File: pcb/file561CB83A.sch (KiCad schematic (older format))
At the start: 50 parts, among them P8 CONN_01X02, P9 CONN_01X02, Q2 BC849, Q3 IRF9530, Q4 CSD18536KCS, Q5 BC849, Q6 BC849, Q7 IRF9530, Q8 CSD18536KCS, Q9 BC849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

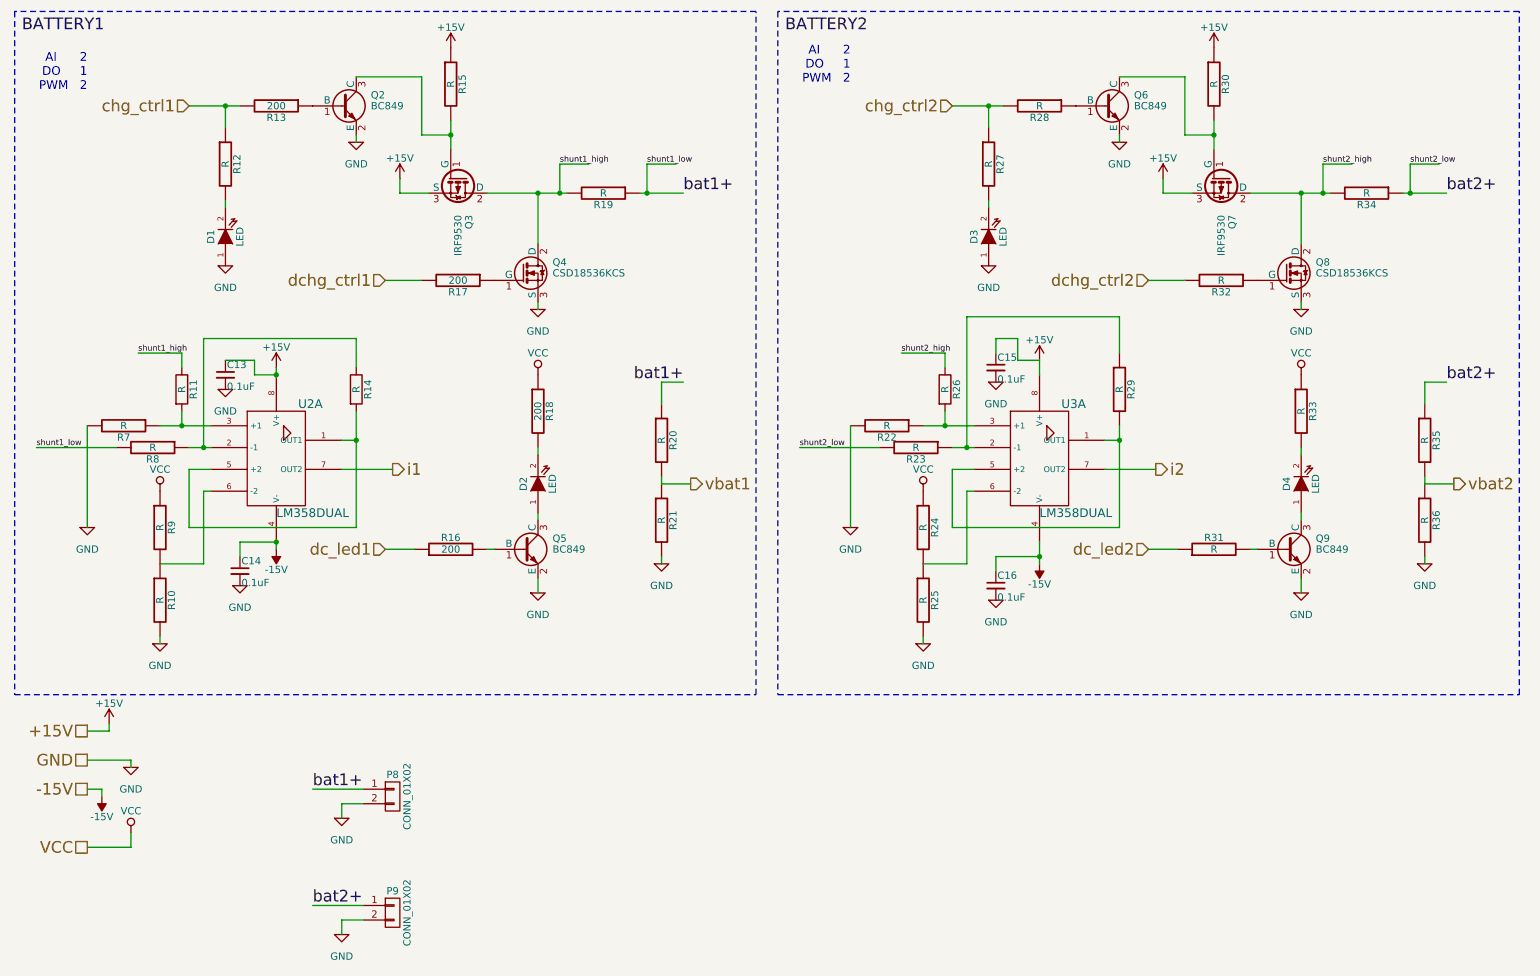
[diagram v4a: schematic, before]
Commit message: Changed fan FET (Q22). Many other minor layout changes. Production candidate.
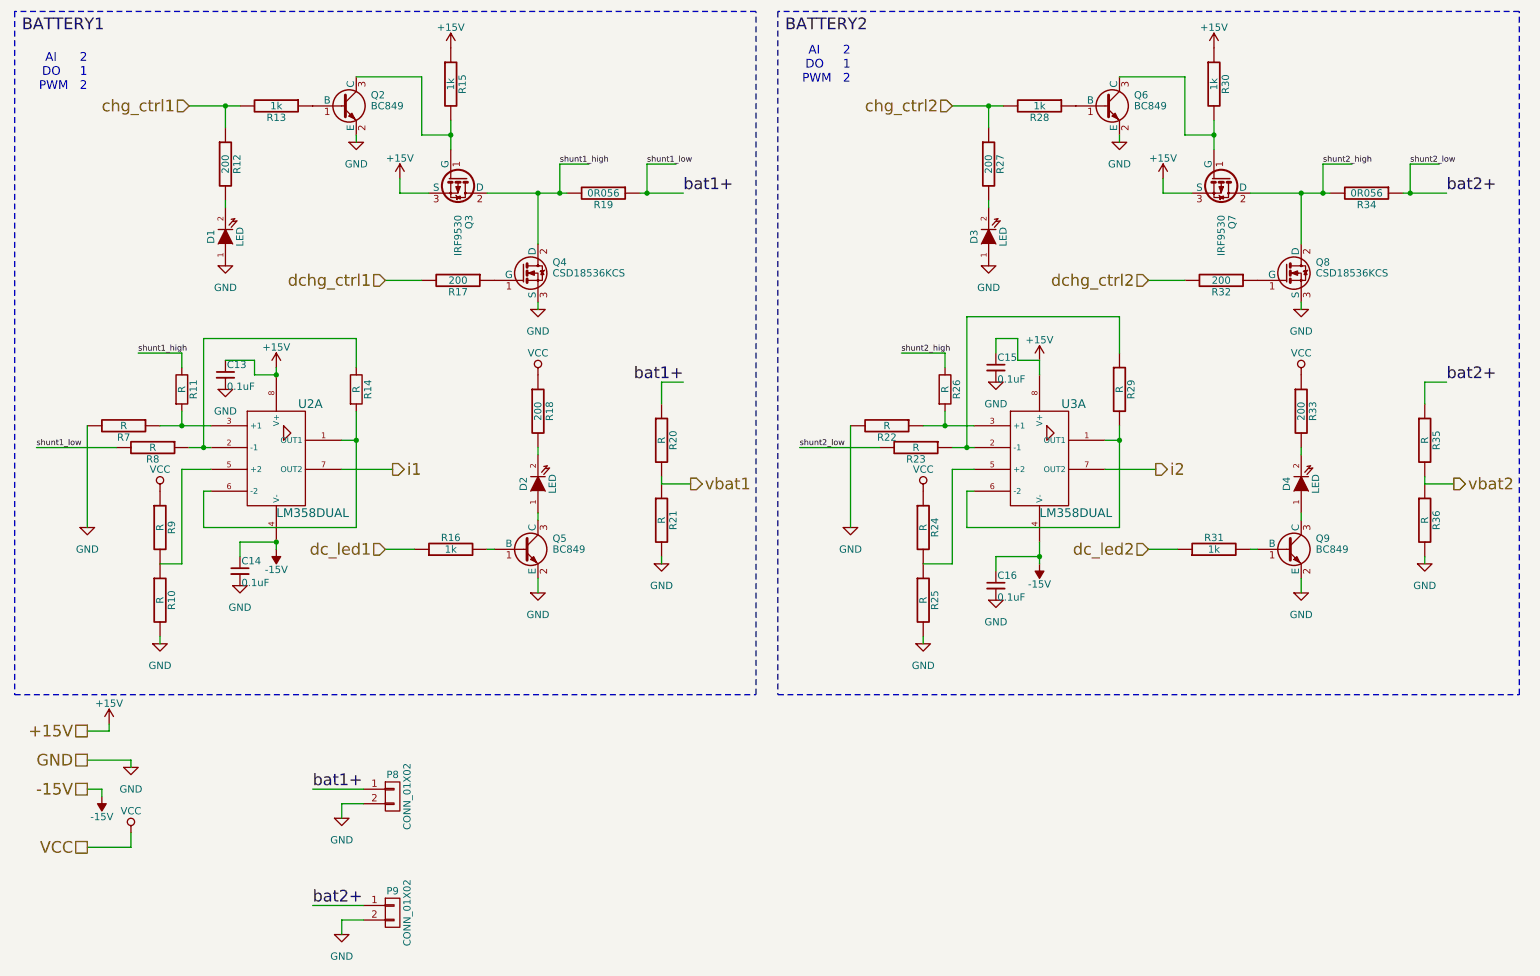
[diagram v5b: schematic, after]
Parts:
- Q3, Q4, Q7, Q8: footprint Power_Integrations:TO-220 -> Custom Footprints:TO-220
- R12, R27, R32, R33: value R -> 200
- R13, R16: value 200 -> 1k
- R15, R28, R30, R31: value R -> 1k
- R19, R34: value R -> 0R056
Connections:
- net at R14.2, U2.1 (OUT1): now also U2.6 (-2); no longer U2.5 (+2)
- net at R10.1, R9.2: now also U2.5 (+2); no longer U2.6 (-2)
- net at R29.2, U3.1 (OUT1): now also U3.6 (-2); no longer U3.5 (+2)
- net at R24.2, R25.1: now also U3.5 (+2); no longer U3.6 (-2)
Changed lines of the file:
@@
 F 0 "Q4" H 4300 2425 50  0000 L CNN
 F 1 "CSD18536KCS" H 4300 2350 50  0000 L CNN
-F 2 "Power_Integrations:TO-220" H 4300 2275 50  0001 L CIN
+F 2 "Custom Footprints:TO-220" H 4300 2275 50  0001 L CIN
 F 3 "" H 4100 2350 50  0000 L CNN
 	1    4100 2350
@@
 F 0 "Q3" H 3900 1775 50  0000 L CNN
 F 1 "IRF9530" H 3900 1700 50  0000 L CNN
-F 2 "Power_Integrations:TO-220" H 3900 1625 50  0001 L CIN
+F 2 "Custom Footprints:TO-220" H 3900 1625 50  0001 L CIN
 F 3 "" H 3650 1700 50  0000 L CNN
 	1    3650 1700
@@
 P 2050 1600
 F 0 "R12" V 2130 1600 50  0000 C CNN
-F 1 "R" V 2050 1600 50  0000 C CNN
+F 1 "200" V 2050 1600 50  0000 C CNN
 F 2 "Resistors_SMD:R_0805_HandSoldering" V 1980 1600 30  0001 C CNN
 F 3 "" H 2050 1600 30  0000 C CNN
@@
 P 3600 1050
 F 0 "R15" V 3680 1050 50  0000 C CNN
-F 1 "R" V 3600 1050 50  0000 C CNN
+F 1 "1k" V 3600 1050 50  0000 C CNN
 F 2 "Resistors_SMD:R_0805_HandSoldering" V 3530 1050 30  0001 C CNN
 F 3 "" H 3600 1050 30  0000 C CNN
@@
 P 4650 1800
 F 0 "R19" V 4730 1800 50  0000 C CNN
-F 1 "R" V 4650 1800 50  0000 C CNN
+F 1 "0R056" V 4650 1800 50  0000 C CNN
 F 2 "Resistors_SMD:R_2512_HandSoldering" V 4580 1800 30  0001 C CNN
 F 3 "" H 4650 1800 30  0000 C CNN
@@
 P 2400 1200
 F 0 "R13" V 2480 1200 50  0000 C CNN
-F 1 "200" V 2400 1200 50  0000 C CNN
+F 1 "1k" V 2400 1200 50  0000 C CNN
 F 2 "Resistors_SMD:R_0805_HandSoldering" V 2330 1200 30  0001 C CNN
 F 3 "" H 2400 1200 30  0000 C CNN
@@
 P 3600 4250
 F 0 "R16" V 3680 4250 50  0000 C CNN
-F 1 "200" V 3600 4250 50  0000 C CNN
+F 1 "1k" V 3600 4250 50  0000 C CNN
 F 2 "Resistors_SMD:R_0805_HandSoldering" V 3530 4250 30  0001 C CNN
 F 3 "" H 3600 4250 30  0000 C CNN
@@
 	1300 3550 750  3550
 Wire Wire Line
-	2950 4100 1800 4100
-Wire Wire Line
-	1800 4100 1800 3700
-Wire Wire Line
-	1800 3700 1950 3700
+	2950 4100 1900 4100
+Wire Wire Line
+	1750 3700 1950 3700
 Connection ~ 2950 3500
 Wire Wire Line
 	1950 3850 1900 3850
-Wire Wire Line
-	1900 3850 1900 4350
-Wire Wire Line
-	1900 4350 1600 4350
 Wire Wire Line
 	1600 4900 1600 4850
@@
 F 0 "Q8" H 9550 2425 50  0000 L CNN
 F 1 "CSD18536KCS" H 9550 2350 50  0000 L CNN
-F 2 "Power_Integrations:TO-220" H 9550 2275 50  0001 L CIN
+F 2 "Custom Footprints:TO-220" H 9550 2275 50  0001 L CIN
 F 3 "" H 9350 2350 50  0000 L CNN
 	1    9350 2350
@@
 F 0 "Q7" H 9150 1775 50  0000 L CNN
 F 1 "IRF9530" H 9150 1700 50  0000 L CNN
-F 2 "Power_Integrations:TO-220" H 9150 1625 50  0001 L CIN
+F 2 "Custom Footprints:TO-220" H 9150 1625 50  0001 L CIN
 F 3 "" H 8900 1700 50  0000 L CNN
 	1    8900 1700
@@
 P 9450 3300
 F 0 "R33" V 9530 3300 50  0000 C CNN
-F 1 "R" V 9450 3300 50  0000 C CNN
+F 1 "200" V 9450 3300 50  0000 C CNN
 F 2 "Resistors_SMD:R_0805_HandSoldering" V 9380 3300 30  0001 C CNN
 F 3 "" H 9450 3300 30  0000 C CNN
@@
 P 7300 1600
 F 0 "R27" V 7380 1600 50  0000 C CNN
-F 1 "R" V 7300 1600 50  0000 C CNN
+F 1 "200" V 7300 1600 50  0000 C CNN
 F 2 "Resistors_SMD:R_0805_HandSoldering" V 7230 1600 30  0001 C CNN
 F 3 "" H 7300 1600 30  0000 C CNN
@@
 P 8850 1050
 F 0 "R30" V 8930 1050 50  0000 C CNN
-F 1 "R" V 8850 1050 50  0000 C CNN
+F 1 "1k" V 8850 1050 50  0000 C CNN
 F 2 "Resistors_SMD:R_0805_HandSoldering" V 8780 1050 30  0001 C CNN
 F 3 "" H 8850 1050 30  0000 C CNN
@@
 P 9900 1800
 F 0 "R34" V 9980 1800 50  0000 C CNN
-F 1 "R" V 9900 1800 50  0000 C CNN
+F 1 "0R056" V 9900 1800 50  0000 C CNN
 F 2 "Resistors_SMD:R_2512_HandSoldering" V 9830 1800 30  0001 C CNN
 F 3 "" H 9900 1800 30  0000 C CNN
@@
 P 7650 1200
 F 0 "R28" V 7730 1200 50  0000 C CNN
-F 1 "R" V 7650 1200 50  0000 C CNN
+F 1 "1k" V 7650 1200 50  0000 C CNN
 F 2 "Resistors_SMD:R_0805_HandSoldering" V 7580 1200 30  0001 C CNN
 F 3 "" H 7650 1200 30  0000 C CNN
@@
 P 8900 2400
 F 0 "R32" V 8980 2400 50  0000 C CNN
-F 1 "R" V 8900 2400 50  0000 C CNN
+F 1 "200" V 8900 2400 50  0000 C CNN
 F 2 "Resistors_SMD:R_0805_HandSoldering" V 8830 2400 30  0001 C CNN
 F 3 "" H 8900 2400 30  0000 C CNN
@@
 P 8850 4250
 F 0 "R31" V 8930 4250 50  0000 C CNN
-F 1 "R" V 8850 4250 50  0000 C CNN
+F 1 "1k" V 8850 4250 50  0000 C CNN
 F 2 "Resistors_SMD:R_0805_HandSoldering" V 8780 4250 30  0001 C CNN
 F 3 "" H 8850 4250 30  0000 C CNN
@@
 	6550 3550 6000 3550
 Wire Wire Line
-	8200 4100 7050 4100
-Wire Wire Line
-	7050 4100 7050 3700
+	7050 3700 7050 4350
 Wire Wire Line
 	7050 3700 7200 3700
@@
 Wire Wire Line
 	7200 3850 7150 3850
-Wire Wire Line
-	7150 3850 7150 4350
-Wire Wire Line
-	7150 4350 6850 4350
 Wire Wire Line
 	6850 4900 6850 4850
@@
 Wire Wire Line
 	7000 3300 7000 3400
+Wire Wire Line
+	1750 3700 1750 4350
+Wire Wire Line
+	1750 4350 1600 4350
+Wire Wire Line
+	1900 3850 1900 4100
+Wire Wire Line
+	7050 4350 6850 4350
+Wire Wire Line
+	8200 4100 7150 4100
+Wire Wire Line
+	7150 4100 7150 3850
 $EndSCHEMATC

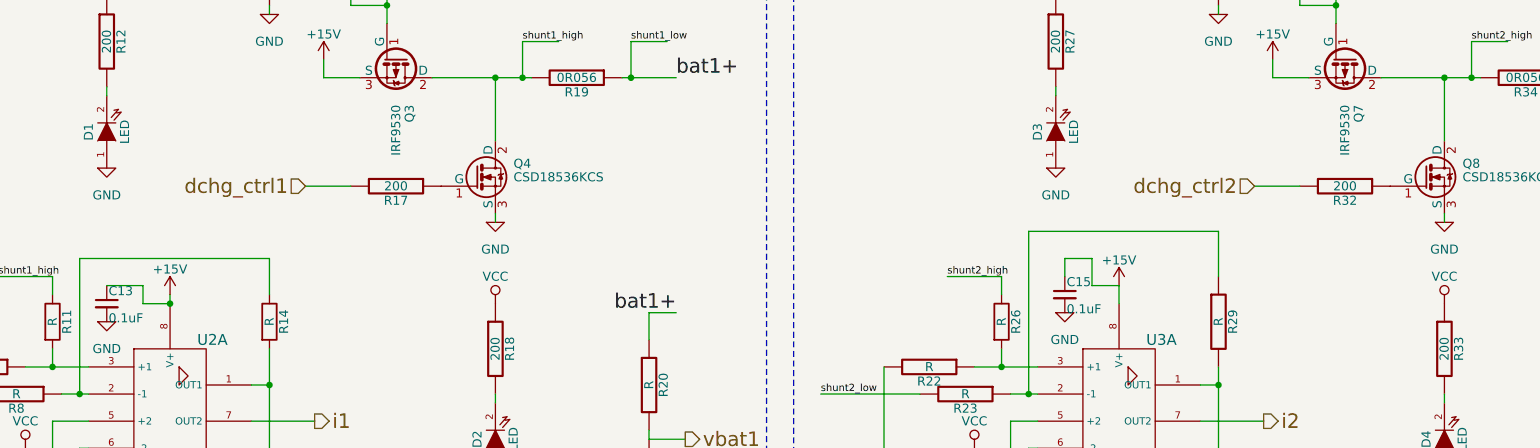
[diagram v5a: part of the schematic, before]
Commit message: Added caps on discharge fet gates
Need to filter the digital signal from the MCU to create an analog
voltage at the gate because the fet should operate in between on and
off states (which generates heat due to high Rds).
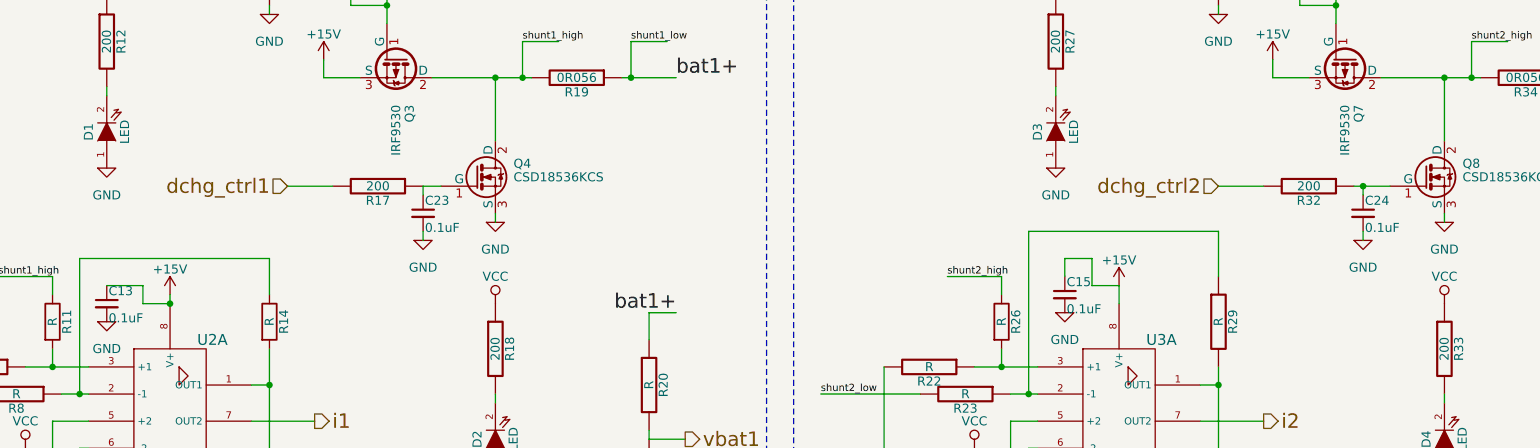
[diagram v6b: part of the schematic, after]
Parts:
- added C23, C24: 0.1uF, Capacitors_SMD:C_0805_HandSoldering, symbol C_Small
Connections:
- net GND: now also C23.2, C24.2
- net at Q4.1 (G), R17.1: now also C23.1
- net at Q8.1 (G), R32.1: now also C24.1
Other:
- moved on the sheet: R17, R32

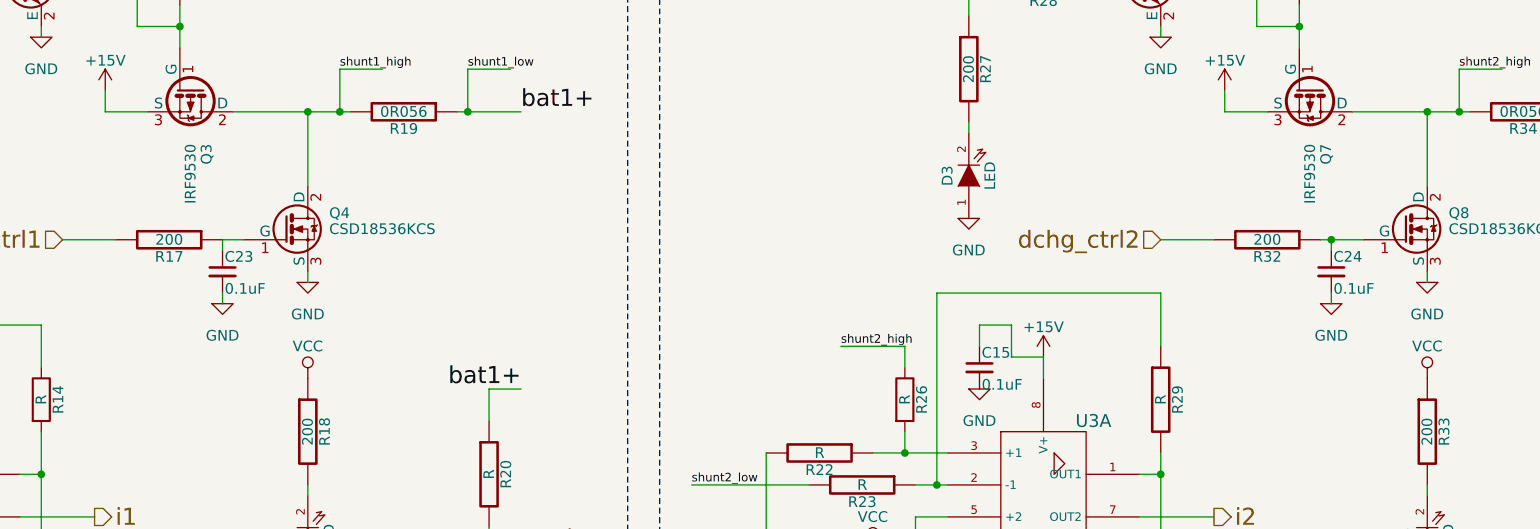
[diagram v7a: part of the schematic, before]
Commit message: Minor package changes.
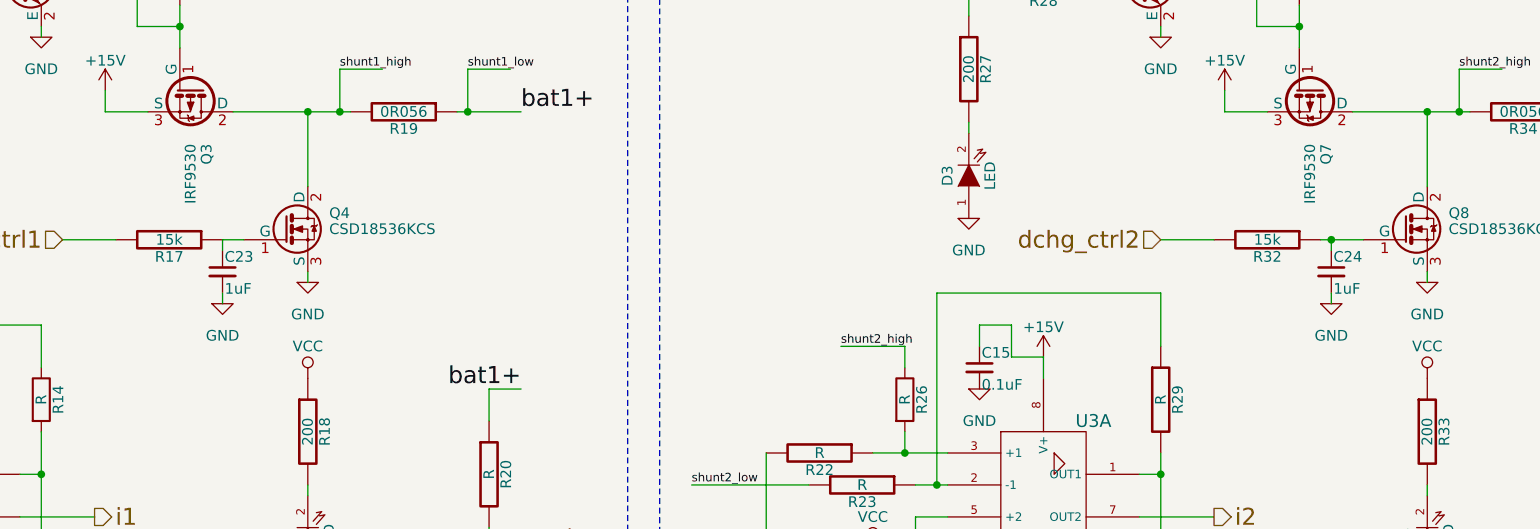
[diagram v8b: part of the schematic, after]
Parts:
- C23, C24: value 0.1uF -> 1uF
- P8, P9: footprint Pin_Headers:Pin_Header_Straight_1x02 -> Custom Footprints:PINHEAD1-2_200mil
- R17, R32: value 200 -> 15k
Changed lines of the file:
@@
 P 3550 2400
 F 0 "R17" V 3630 2400 50  0000 C CNN
-F 1 "200" V 3550 2400 50  0000 C CNN
+F 1 "15k" V 3550 2400 50  0000 C CNN
 F 2 "Resistors_SMD:R_0805_HandSoldering" V 3480 2400 30  0001 C CNN
 F 3 "" H 3550 2400 30  0000 C CNN
@@
 P 8700 2400
 F 0 "R32" V 8780 2400 50  0000 C CNN
-F 1 "200" V 8700 2400 50  0000 C CNN
+F 1 "15k" V 8700 2400 50  0000 C CNN
 F 2 "Resistors_SMD:R_0805_HandSoldering" V 8630 2400 30  0001 C CNN
 F 3 "" H 8700 2400 30  0000 C CNN
@@
 F 0 "P8" H 3200 6100 50  0000 C CNN
 F 1 "CONN_01X02" V 3300 5950 50  0000 C CNN
-F 2 "Pin_Headers:Pin_Header_Straight_1x02" H 3200 5950 60  0001 C CNN
+F 2 "Custom Footprints:PINHEAD1-2_200mil" H 3200 5950 60  0001 C CNN
 F 3 "" H 3200 5950 60  0000 C CNN
 	1    3200 5950
@@
 F 0 "P9" H 3200 6900 50  0000 C CNN
 F 1 "CONN_01X02" V 3300 6750 50  0000 C CNN
-F 2 "Pin_Headers:Pin_Header_Straight_1x02" H 3200 6750 60  0001 C CNN
+F 2 "Custom Footprints:PINHEAD1-2_200mil" H 3200 6750 60  0001 C CNN
 F 3 "" H 3200 6750 60  0000 C CNN
 	1    3200 6750
@@
 P 3800 2550
 F 0 "C23" H 3810 2620 50  0000 L CNN
-F 1 "0.1uF" H 3810 2470 50  0000 L CNN
+F 1 "1uF" H 3810 2470 50  0000 L CNN
 F 2 "Capacitors_SMD:C_0805_HandSoldering" H 3800 2550 60  0001 C CNN
 F 3 "" H 3800 2550 60  0000 C CNN
@@
 P 9000 2550
 F 0 "C24" H 9010 2620 50  0000 L CNN
-F 1 "0.1uF" H 9010 2470 50  0000 L CNN
+F 1 "1uF" H 9010 2470 50  0000 L CNN
 F 2 "Capacitors_SMD:C_0805_HandSoldering" H 9000 2550 60  0001 C CNN
 F 3 "" H 9000 2550 60  0000 C CNN
